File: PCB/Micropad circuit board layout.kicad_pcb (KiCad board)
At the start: 2 copper layers, 96 x 56 mm, 47 parts, among them SW1 SW_Push_45deg, SW10 SW_Push_45deg, SW11 SW_Push_45deg, SW12 SW_Push_45deg, SW13 SW_Push_45deg, SW14 SW_Push_45deg, SW15 SW_Push_45deg, SW2 SW_Push_45deg, SW3 SW_Push_45deg, SW4 SW_Push_45deg, SW5 SW_Push_45deg, SW6 SW_Push_45deg, SW7 SW_Push_45deg, SW8 SW_Push_45deg, SW9 SW_Push_45deg, U1 MOUDLE-SEEEDUINO-XIAO

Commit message: Fixing files
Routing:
- net /Row_1: track 123.5 -> 114.1 mm
- net Net-(D8-A): track 5.78 -> 0.00 mm
- net /Row_0: track 95.9 -> 93.8 mm
- net /Col_1: track 54.5 -> 55.4 mm
- removed copper zone on B.Cu, net (none)
- removed copper zone on F.Cu, net (none)
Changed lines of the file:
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@@
 			(disableapertmacros no)
 			(usegerberextensions yes)
-			(usegerberattributes yes)
-			(usegerberadvancedattributes yes)
-			(creategerberjobfile yes)
+			(usegerberattributes no)
+			(usegerberadvancedattributes no)
+			(creategerberjobfile no)
 			(dashed_line_dash_ratio 12.000000)
 			(dashed_line_gap_ratio 3.000000)
@@
 			(sketchdnponfab yes)
 			(crossoutdnponfab yes)
-			(subtractmaskfromsilk no)
+			(subtractmaskfromsilk yes)
 			(outputformat 1)
 			(mirror no)
 			(drillshape 0)
 			(scaleselection 1)
-			(outputdirectory "../../")
+			(outputdirectory "../Gerbers/")
 		)
 	)
@@
 	)
 	(segment
-		(start 160.075 80.439)
-		(end 157.975 80.439)
-		(width 0.2)
-		(layer "B.Cu")
-		(net 2)
-	)
-	(segment
 		(start 164.33475 80.439)
 		(end 164.71375 80.06)
@@
 	)
 	(segment
-		(start 142.285 80.06)
-		(end 133.47 80.06)
+		(start 133.47 80.06)
+		(end 145.66375 80.06)
 		(width 0.2)
 		(layer "B.Cu")
@@
 	(segment
 		(start 153.699 80.439)
-		(end 158.401 80.439)
+		(end 164.33475 80.439)
 		(width 0.2)
 		(layer "B.Cu")
@@
 	)
 	(segment
-		(start 158.401 80.439)
-		(end 164.33475 80.439)
-		(width 0.2)
-		(layer "B.Cu")
-		(net 2)
-	)
-	(segment
 		(start 132.115 78.705)
 		(end 132.115 77.945)
@@
 	)
 	(segment
-		(start 142.285 80.06)
-		(end 145.66375 80.06)
-		(width 0.2)
-		(layer "B.Cu")
-		(net 2)
-	)
-	(segment
 		(start 164.71375 80.06)
 		(end 183.76375 80.06)
@@
 	)
 	(segment
-		(start 135.94625 101.8)
-		(end 142.97375 101.8)
-		(width 0.2)
-		(layer "B.Cu")
-		(net 3)
-	)
-	(segment
 		(start 129.935 95.78875)
 		(end 135.94625 101.8)
@@
 	)
 	(segment
-		(start 162.02375 101.8)
-		(end 168.035 95.78875)
-		(width 0.2)
-		(layer "B.Cu")
-		(net 3)
-	)
-	(segment
 		(start 149.13 100.805)
 		(end 148.135 101.8)
@@
 	)
 	(segment
-		(start 148.985 100.135)
-		(end 148.985 100.95)
-		(width 0.2)
-		(layer "B.Cu")
-		(net 3)
-	)
-	(segment
-		(start 142.97375 101.8)
+		(start 135.94625 101.8)
 		(end 148.135 101.8)
 		(width 0.2)
@@
 	)
 	(segment
-		(start 162.02375 101.8)
-		(end 181.07375 101.8)
-		(width 0.2)
-		(layer "B.Cu")
-		(net 3)
-	)
-	(segment
 		(start 131.07724 75.405)
 		(end 128.834 77.64824)
@@
 	(segment
 		(start 148.135 101.8)
-		(end 162.02375 101.8)
+		(end 181.07375 101.8)
 		(width 0.2)
 		(layer "B.Cu")
@@
 	)
 	(segment
-		(start 141.975 82.836)
+		(start 141.975 66.445)
 		(end 141.975 104.495)
 		(width 0.2)
@@
 	)
 	(segment
-		(start 141.96984 82.836)
-		(end 141.975 82.836)
-		(width 0.2)
-		(layer "F.Cu")
-		(net 21)
-	)
-	(segment
-		(start 141.975 66.445)
-		(end 141.975 80.634)
-		(width 0.2)
-		(layer "F.Cu")
-		(net 21)
-	)
-	(segment
-		(start 141.975 80.634)
-		(end 141.96984 80.634)
-		(width 0.2)
-		(layer "F.Cu")
-		(net 21)
-	)
-	(segment
 		(start 142 66.42)
 		(end 141.975 66.445)
@@
 	)
 	(segment
-		(start 141.975 82.836)
-		(end 141.975 80.634)
-		(width 0.2)
-		(layer "F.Cu")
-		(net 21)
-	)
-	(segment
 		(start 145.741 78.861)
 		(end 147.365 80.485)
@@
 	)
 	(segment
+		(start 155.258686 66.42)
+		(end 148.813686 72.865)
+		(width 0.2)
+		(layer "F.Cu")
+		(net 22)
+	)
+	(segment
+		(start 162.235 67.605)
+		(end 162.235 84.285)
+		(width 0.2)
+		(layer "F.Cu")
+		(net 22)
+	)
+	(segment
 		(start 161.05 66.42)
-		(end 161.05 85.47)
+		(end 162.235 67.605)
 		(width 0.2)
 		(layer "F.Cu")
@@
 	)
 	(segment
-		(start 155.258686 66.42)
-		(end 148.813686 72.865)
+		(start 162.235 84.285)
+		(end 161.05 85.47)
 		(width 0.2)
 		(layer "F.Cu")
@@
 	)
 	(segment
-		(start 197.3721 64.075)
-		(end 197.3411 64.044)
-		(width 0.2)
-		(layer "F.Cu")
-		(net 25)
-	)
-	(segment
 		(start 218.2 66.42)
 		(end 215.824 64.044)
@@
 	)
 	(segment
-		(start 133.605 79.305)
-		(end 133.715 79.415)
-		(width 0.2)
-		(layer "F.Cu")
-		(net 26)
-	)
-	(segment
 		(start 132.115 80.485)
 		(end 132.645 80.485)
@@
 	)
 	(segment
-		(start 175.145 78.93)
-		(end 175.145 78.92)
-		(width 0.2)
-		(layer "B.Cu")
-		(net 33)
-	)
-	(segment
 		(start 181.12 98.9)
 		(end 182.53 97.49)
@@
 	)
 	(segment
-		(start 168.19375 88.01)
-		(end 168.035 88.16875)
-		(width 0.2)
-		(layer "B.Cu")
-		(net 43)
-	)
-	(segment
-		(start 173.75 88.01)
-		(end 168.19375 88.01)
-		(width 0.2)
-		(layer "B.Cu")
-		(net 43)
-	)
-	(segment
 		(start 173.75 107.06)
 		(end 168.19375 107.06)
@@
 		(net 44)
 	)
-	(zone
-		(net 0)
-		(net_name "")
-		(layers "F.Cu" "B.Cu")
-		(hatch edge 0.5)
-		(connect_pads
-			(clearance 0.5)
-		)
-		(min_thickness 0.25)
-		(filled_areas_thickness no)
-		(fill yes
-			(thermal_gap 0.5)
-			(thermal_bridge_width 0.5)
-			(island_removal_mode 1)
-			(island_area_min 10)
-		)
-		(polygon
-			(pts
-				(xy 227.475 59.515) (xy 122.475 59.515) (xy 122.475 119.515) (xy 227.475 119.515)
-			)
-		)
-	)
 	(embedded_fonts no)

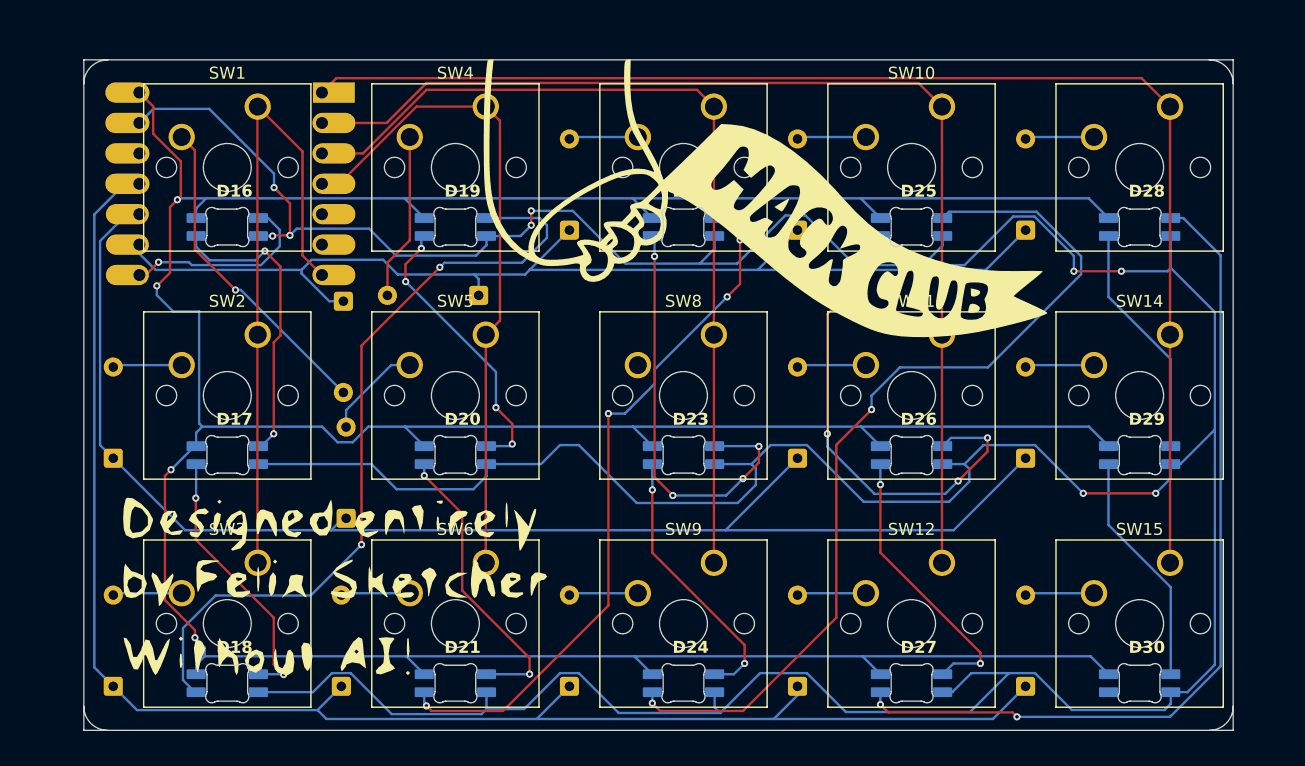
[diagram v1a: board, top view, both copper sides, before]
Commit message: Added a filled zone on the PCB
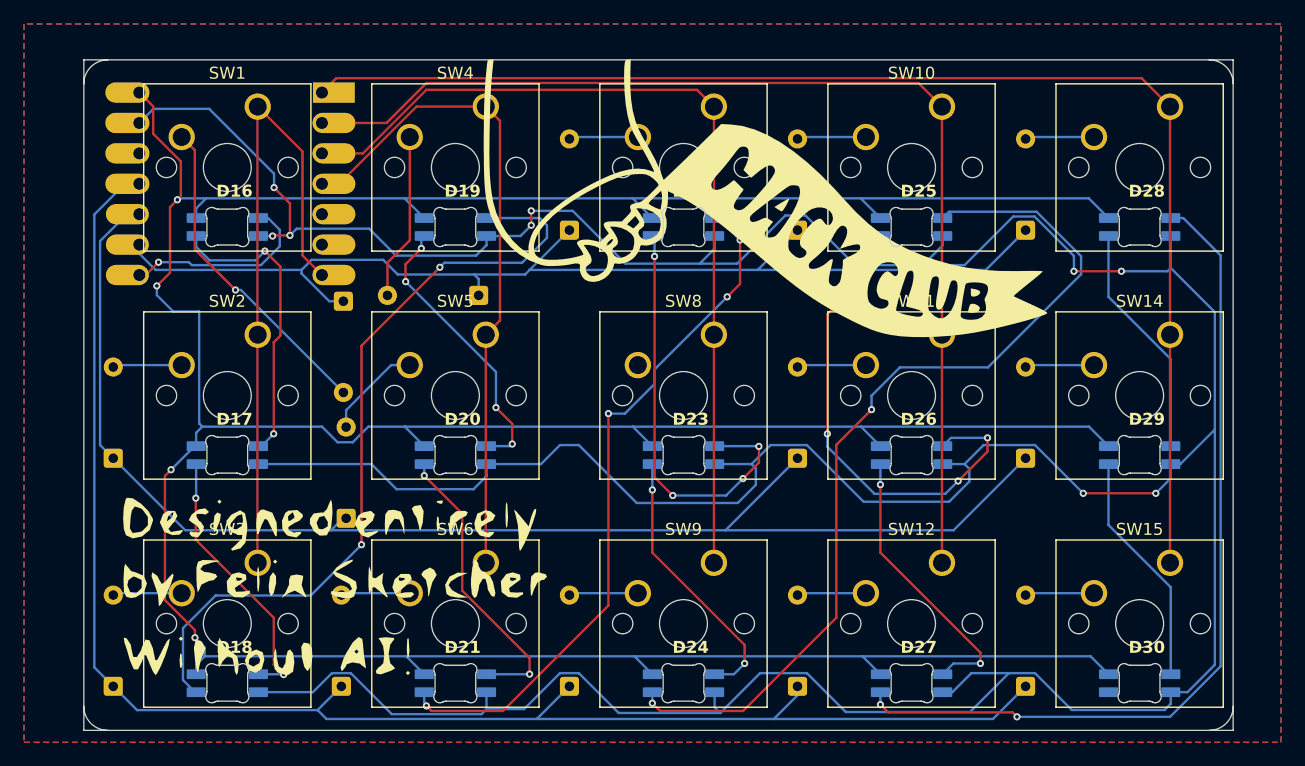
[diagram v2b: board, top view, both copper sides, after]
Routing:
- added copper zone on B.Cu, net (none)
- added copper zone on F.Cu, net (none)
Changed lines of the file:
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@@
 		(net 44)
+	)
+	(zone
+		(net 0)
+		(net_name "")
+		(layers "F.Cu" "B.Cu")
+		(hatch edge 0.5)
+		(connect_pads
+			(clearance 0.5)
+		)
+		(min_thickness 0.25)
+		(filled_areas_thickness no)
+		(fill yes
+			(thermal_gap 0.5)
+			(thermal_bridge_width 0.5)
+			(island_removal_mode 1)
+			(island_area_min 10)
+		)
+		(polygon
+			(pts
+				(xy 227.475 59.515) (xy 122.475 59.515) (xy 122.475 119.515) (xy 227.475 119.515)
+			)
+		)
 	)
 	(embedded_fonts no)
